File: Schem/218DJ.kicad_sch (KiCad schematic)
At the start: 40 parts, among them J1 5V_IN, SW45 ENC1, SW46 ENC2, SW47 ENC3, SW48 ENC4, SW5 SW_SPST, SW50 JOG1, SW51 JOG2, U1 74HCT125, U2 CD74HC4067M, U2 Teensy4.0, U3 CD74HC4067M

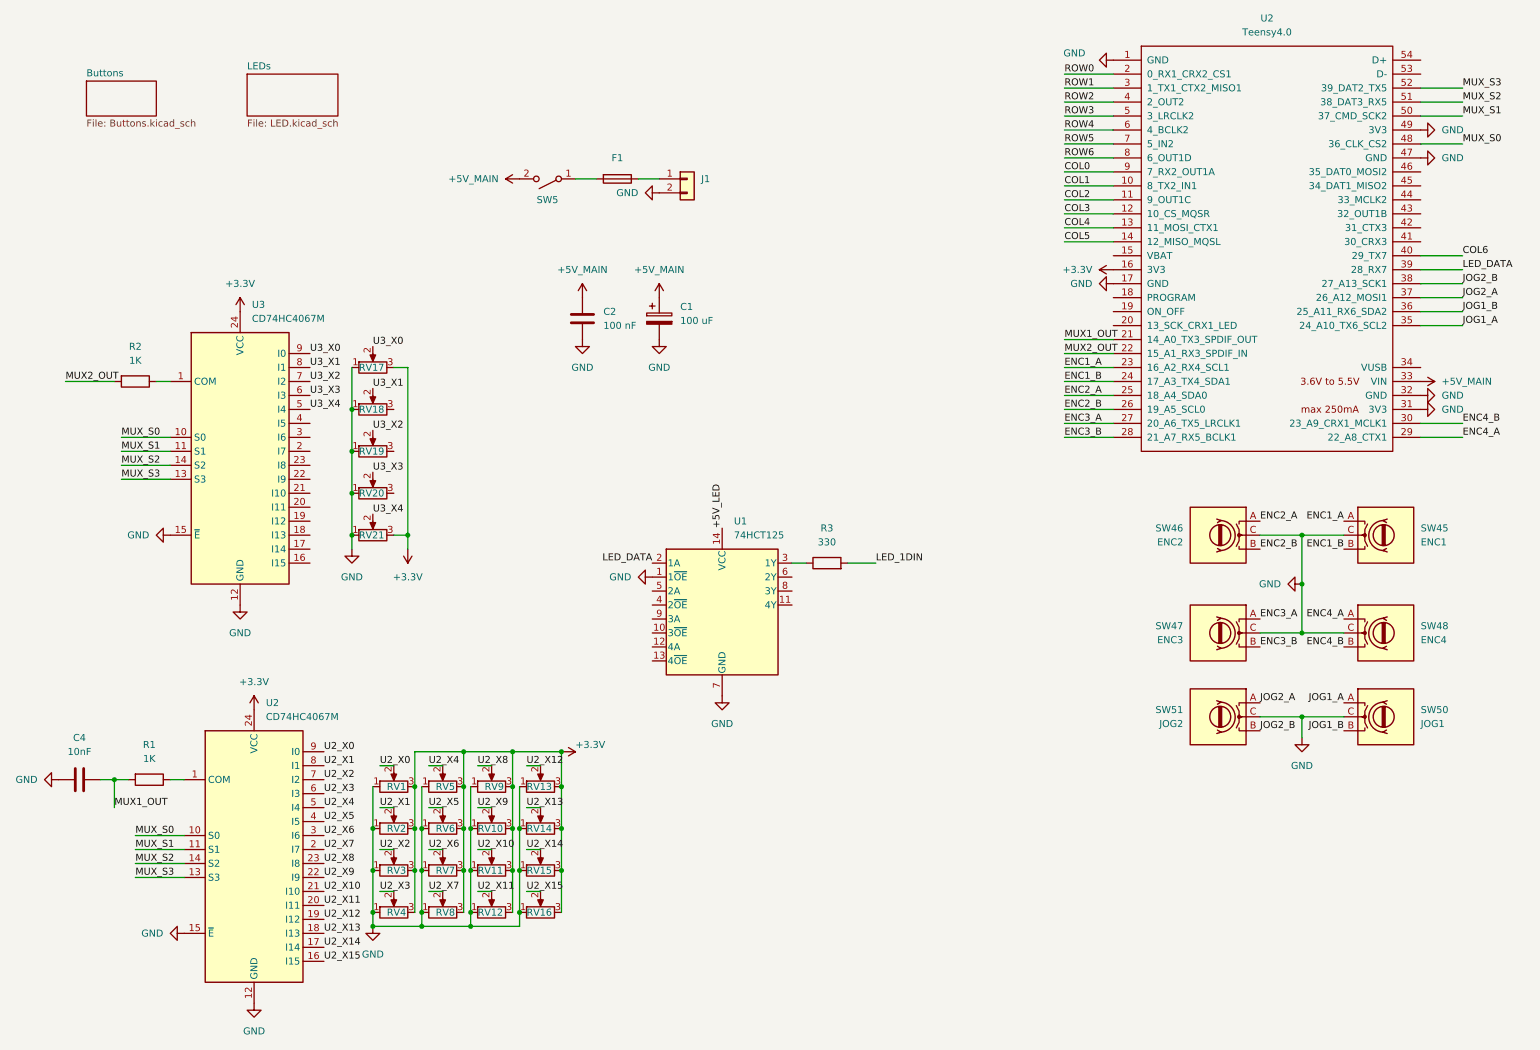
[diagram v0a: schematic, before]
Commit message: Update Schematic fixing errors (consult journal)
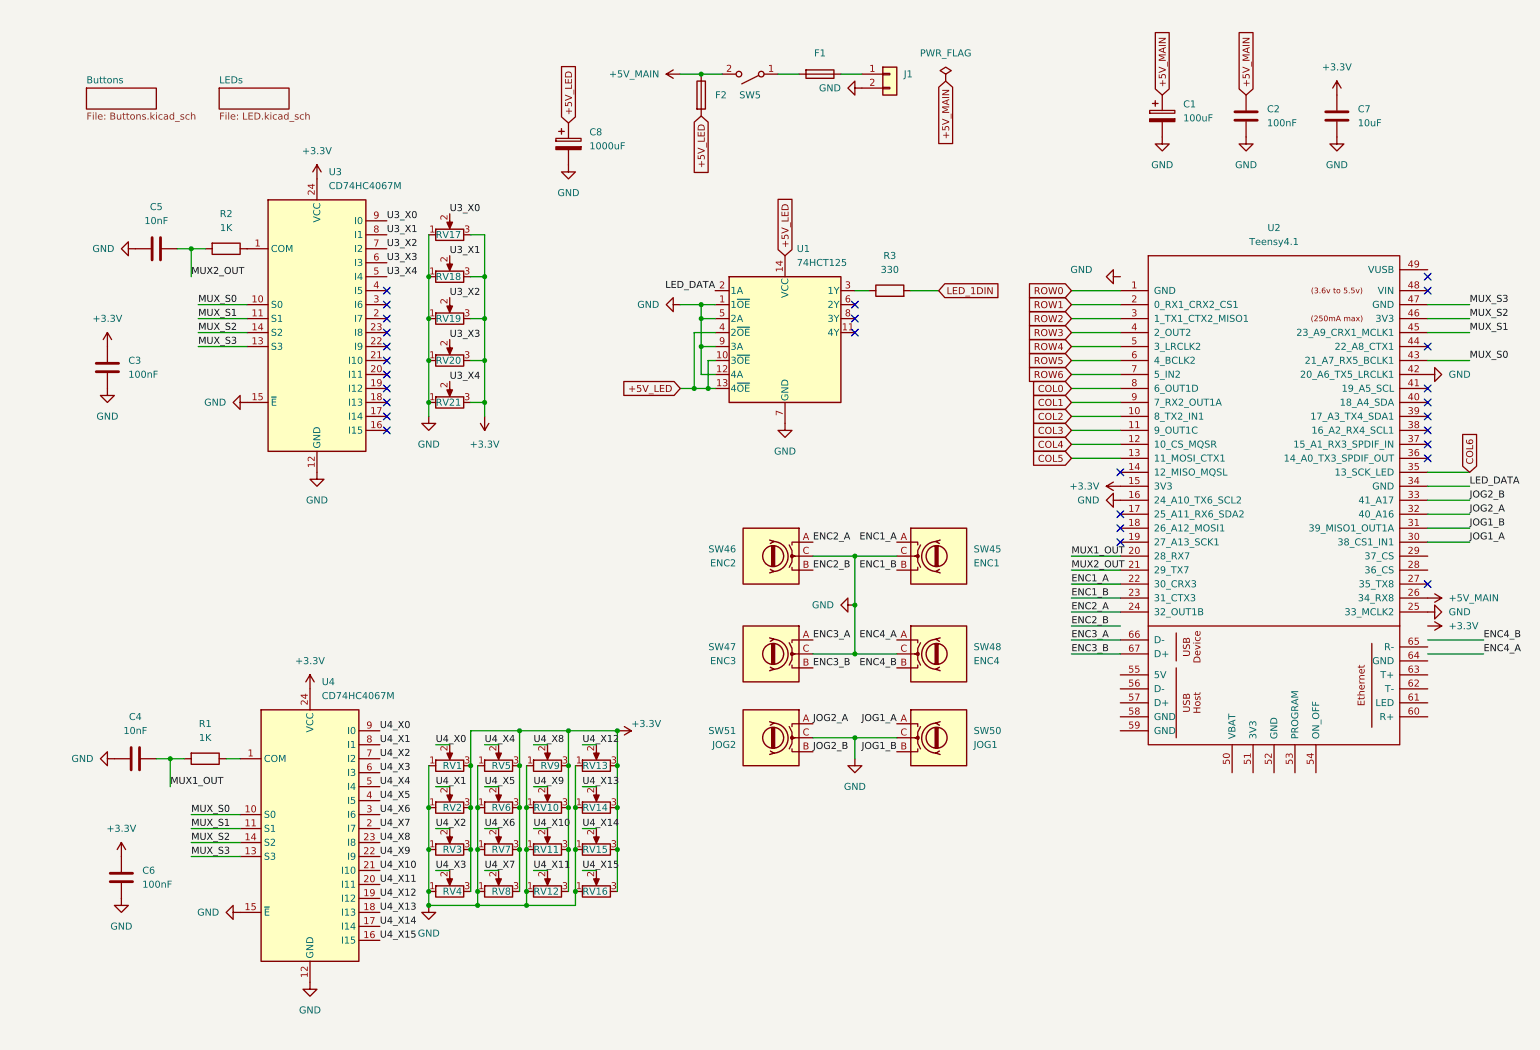
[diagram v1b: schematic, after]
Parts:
- removed U2: Teensy4.0, symbol teensy:Teensy4.0
- added C3, C6: 100nF, symbol Device:C
- added C5: 10nF, symbol Device:C
- added C7: 10uF, symbol Device:C
- added C8: 1000uF, symbol Device:C_Polarized
- added F2: Fuse, symbol Device:Fuse
- added U2: Teensy4.1, symbol teensy:Teensy4.1
- C1: value 100 uF -> 100uF
- C2: value 100 nF -> 100nF
- renumbered U2 to U4
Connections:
- net +3.3V: now also RV18.3, RV19.3, RV20.3, C3.1, C6.1, C7.1, U2.15 (3V3)
- net +5V_LED: now also U1.10 (3~{OE}), U1.13 (4~{OE}), U1.4 (2~{OE}), C8.1, F2.2
- net +5V_MAIN: now also F2.1, U2.26 (34_RX8)
- net COL0: now also U2.8 (6_OUT1D)
- net COL1: now also U2.9 (7_RX2_OUT1A)
- net COL2: now also U2.10 (8_TX2_IN1)
- net COL3: now also U2.11 (9_OUT1C)
- net COL4: now also U2.12 (10_CS_MQSR)
- net COL5: now also U2.13 (11_MOSI_CTX1)
- net COL6: now also U2.35 (13_SCK_LED)
- net ENC1_A: now also U2.22 (30_CRX3)
- net ENC1_B: now also U2.23 (31_CTX3)
- net ENC2_A: now also U2.24 (32_OUT1B)
- net ENC3_A: now also U2.66 (D-)
- net ENC3_B: now also U2.67 (D+)
- net GND: now also U1.12 (4A), U1.5 (2A), U1.9 (3A), C3.2, C5.1, C6.2, C7.2, C8.2, U2.16 (24_A10_TX6_SCL2), U2.25 (33_MCLK2), U2.42 (20_A6_TX5_LRCLK1)
- net JOG1_A: now also U2.30 (38_CS1_IN1)
- net JOG1_B: now also U2.31 (39_MISO1_OUT1A)
- net JOG2_A: now also U2.32 (40_A16)
- net JOG2_B: now also U2.33 (41_A17)
- net LED_DATA: now also U2.34 (GND)
- net MUX1_OUT: now also U2.20 (28_RX7)
- net MUX2_OUT: now also C5.2, U2.21 (29_TX7)
- net MUX_S0: now also U2.43 (21_A7_RX5_BCLK1)
- net MUX_S1: now also U2.45 (23_A9_CRX1_MCLK1)
- net MUX_S2: now also U2.46 (3V3)
- net MUX_S3: now also U2.47 (GND)
- net ROW0: now also U2.1 (GND)
- net ROW1: now also U2.2 (0_RX1_CRX2_CS1)
- net ROW2: now also U2.3 (1_TX1_CTX2_MISO1)
- net ROW3: now also U2.4 (2_OUT2)
- net ROW4: now also U2.5 (3_LRCLK2)
- net ROW5: now also U2.6 (4_BCLK2)
- net ROW6: now also U2.7 (5_IN2)
- net U2_X0 renamed U4_X0
- net U2_X1 renamed U4_X1
- net U2_X10 renamed U4_X10
- net U2_X11 renamed U4_X11
- net U2_X12 renamed U4_X12
- net U2_X13 renamed U4_X13
- net U2_X14 renamed U4_X14
- net U2_X15 renamed U4_X15
- net U2_X2 renamed U4_X2
- net U2_X3 renamed U4_X3
- net U2_X4 renamed U4_X4
- net U2_X5 renamed U4_X5
- net U2_X6 renamed U4_X6
- net U2_X7 renamed U4_X7
- net U2_X8 renamed U4_X8
- net U2_X9 renamed U4_X9
- no-connect marks 0 -> 28
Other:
- moved on the sheet: C4, F1, J1, R1, R3, RV1, RV10, RV11, RV12, RV13, RV14, RV15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

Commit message: Update schematic with magnetic rotary sensors and updated board
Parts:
- removed SW50: JOG1, symbol Device:RotaryEncoder
- removed SW51: JOG2, symbol Device:RotaryEncoder
- added U5: JOG_1, Package_SO:TSSOP-14_4.4x5mm_P0.65mm, symbol Sensor_Magnetic:AS5047D
- added U6: JOG_2, Package_SO:TSSOP-14_4.4x5mm_P0.65mm, symbol Sensor_Magnetic:AS5047D
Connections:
- net +3.3V: now also U2.46 (3V3), U5.1 (~{CS}), U5.11 (VDD), U5.12 (VDD3V3), U6.1 (~{CS}), U6.11 (VDD), U6.12 (VDD3V3); no longer U2.15 (3V3)
- net +5V_MAIN: now also U2.48 (VIN); no longer U2.26 (34_RX8)
- net COL0: now also U2.11 (9_OUT1C); no longer U2.8 (6_OUT1D)
- net COL1: now also U2.12 (10_CS_MQSR); no longer U2.9 (7_RX2_OUT1A)
- net COL2: now also U2.13 (11_MOSI_CTX1); no longer U2.10 (8_TX2_IN1)
- net COL3: now also U2.14 (12_MISO_MQSL); no longer U2.11 (9_OUT1C)
- net COL4: now also U2.16 (24_A10_TX6_SCL2); no longer U2.12 (10_CS_MQSR)
- net COL5: now also U2.17 (25_A11_RX6_SDA2); no longer U2.13 (11_MOSI_CTX1)
- net COL6: now also U2.18 (26_A12_MOSI1); no longer U2.35 (13_SCK_LED)
- net ENC1_A: now also U2.38 (16_A2_RX4_SCL1); no longer U2.22 (30_CRX3)
- net ENC1_B: now also U2.39 (17_A3_TX4_SDA1); no longer U2.23 (31_CTX3)
- net ENC2_A: now also U2.20 (28_RX7); no longer U2.24 (32_OUT1B)
- net ENC2_B: now also U2.21 (29_TX7)
- net ENC3_A: now also U2.22 (30_CRX3); no longer U2.66 (D-)
- net ENC3_B: now also U2.23 (31_CTX3); no longer U2.67 (D+)
- net ENC4_A: now also U2.24 (32_OUT1B)
- net ENC4_B: now also U2.25 (33_MCLK2)
- net GND: now also U2.1 (GND), U2.34 (GND), U2.47 (GND), U5.13 (GND), U5.2 (CLK), U5.4 (MOSI), U5.5 (TST), U6.13 (GND), U6.2 (CLK), U6.4 (MOSI), U6.5 (TST); no longer U2.16 (24_A10_TX6_SCL2), U2.25 (33_MCLK2), U2.42 (20_A6_TX5_LRCLK1)
- net JOG1_A: now also U2.26 (34_RX8), U5.7 (A); no longer U2.30 (38_CS1_IN1)
- net JOG1_B: now also U2.27 (35_TX8), U5.6 (B); no longer U2.31 (39_MISO1_OUT1A)
- net JOG2_A: now also U2.28 (36_CS), U6.7 (A); no longer U2.32 (40_A16)
- net JOG2_B: now also U2.29 (37_CS), U6.6 (B); no longer U2.33 (41_A17)
- net LED_DATA: now also U2.44 (22_A8_CTX1); no longer U2.34 (GND)
- net MUX1_OUT: now also U2.36 (14_A0_TX3_SPDIF_OUT); no longer U2.20 (28_RX7)
- net MUX2_OUT: now also U2.37 (15_A1_RX3_SPDIF_IN); no longer U2.21 (29_TX7)
- net MUX_S0: now also U2.30 (38_CS1_IN1); no longer U2.43 (21_A7_RX5_BCLK1)
- net MUX_S1: now also U2.31 (39_MISO1_OUT1A); no longer U2.45 (23_A9_CRX1_MCLK1)
- net MUX_S2: now also U2.32 (40_A16); no longer U2.46 (3V3)
- net MUX_S3: now also U2.33 (41_A17); no longer U2.47 (GND)
- net ROW0: now also U2.2 (0_RX1_CRX2_CS1); no longer U2.1 (GND)
- net ROW1: now also U2.3 (1_TX1_CTX2_MISO1); no longer U2.2 (0_RX1_CRX2_CS1)
- net ROW2: now also U2.4 (2_OUT2); no longer U2.3 (1_TX1_CTX2_MISO1)
- net ROW3: now also U2.5 (3_LRCLK2); no longer U2.4 (2_OUT2)
- net ROW4: now also U2.6 (4_BCLK2); no longer U2.5 (3_LRCLK2)
- net ROW5: now also U2.7 (5_IN2); no longer U2.6 (4_BCLK2)
- net ROW6: now also U2.8 (6_OUT1D); no longer U2.7 (5_IN2)
- no-connect marks 28 -> 53
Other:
- moved on the sheet: C4, C6, R1, R3, RV1, RV10, RV11, RV12, RV13, RV14, RV15, RV16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
